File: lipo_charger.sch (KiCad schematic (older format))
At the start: 13 parts, among them P1 CONN_01X02, P2 CONN_01X02, Q1 BC557, Q2 BC547, U1 MCP73831

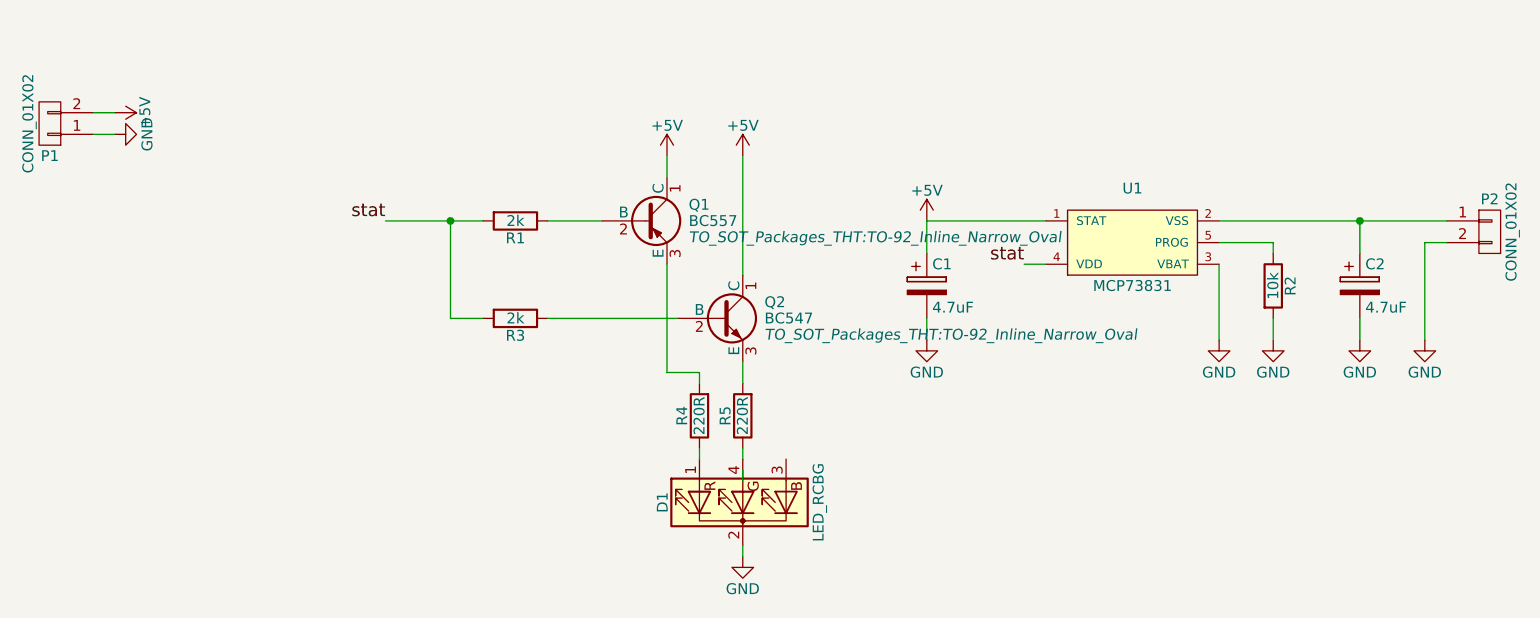
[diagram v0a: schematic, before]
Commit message: 3x lipo charger with tracks
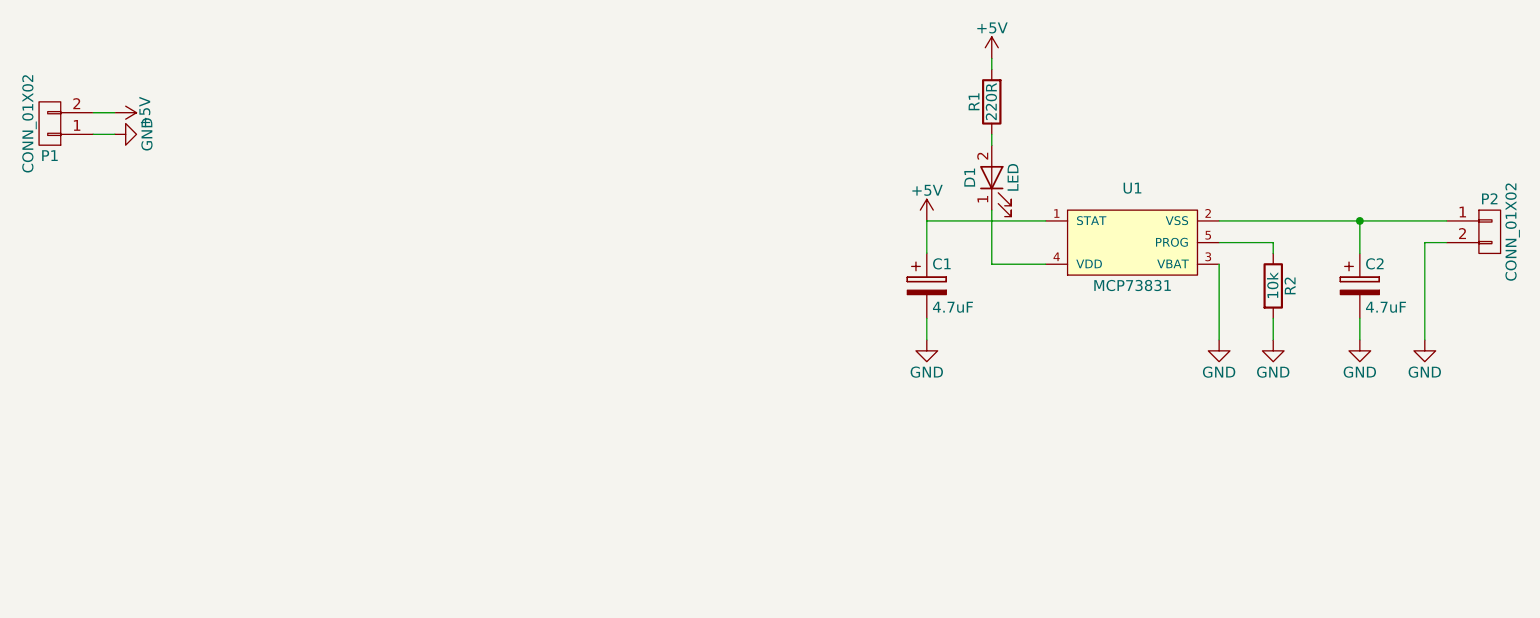
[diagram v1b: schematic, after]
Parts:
- removed D1: LED_RCBG, LEDs:LED_D5.0mm-4, symbol LED_RCBG
- removed Q1: BC557, TO_SOT_Packages_THT:TO-92_Inline_Narrow_Oval, symbol BC557
- removed Q2: BC547, TO_SOT_Packages_THT:TO-92_Inline_Narrow_Oval, symbol BC547
- removed R3: 2k, Resistors_ThroughHole:R_Axial_DIN0204_L3.6mm_D1.6mm_P5.08mm_Horizontal, symbol R
- removed R4, R5: 220R, Resistors_ThroughHole:R_Axial_DIN0204_L3.6mm_D1.6mm_P5.08mm_Horizontal, symbol R
- added D1: LED, LEDs:LED_D3.0mm, symbol LED
- P2: footprint borniers:bornier2_V -> Pin_Headers:Pin_Header_Straight_1x02_Pitch2.54mm
- R1: value 2k -> 220R
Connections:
- net labels removed: stat
- wire segments 30 -> 18
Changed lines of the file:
@@
 $EndDescr
-$Comp
-L LED_RCBG D1
-U 1 1 58917860
-P 4200 2600
-F 0 "D1" H 4200 2970 50  0000 C CNN
-F 1 "LED_RCBG" H 4200 2250 50  0000 C CNN
-F 2 "LEDs:LED_D5.0mm-4" H 4200 2550 50  0001 C CNN
-F 3 "" H 4200 2550 50  0000 C CNN
-	1    4200 2600
-	0    -1   -1   0
-$EndComp
-$Comp
-L R R1
-U 1 1 58917A5E
-P 3150 1300
-F 0 "R1" V 3230 1300 50  0000 C CNN
-F 1 "2k" V 3150 1300 50  0000 C CNN
-F 2 "Resistors_ThroughHole:R_Axial_DIN0204_L3.6mm_D1.6mm_P5.08mm_Horizontal" V 3080 1300 50  0001 C CNN
-F 3 "" H 3150 1300 50  0000 C CNN
-	1    3150 1300
-	0    1    1    0
-$EndComp
-$Comp
-L R R4
-U 1 1 58918266
-P 4000 2200
-F 0 "R4" V 4080 2200 50  0000 C CNN
-F 1 "220R" V 4000 2200 50  0000 C CNN
-F 2 "Resistors_ThroughHole:R_Axial_DIN0204_L3.6mm_D1.6mm_P5.08mm_Horizontal" V 3930 2200 50  0001 C CNN
-F 3 "" H 4000 2200 50  0000 C CNN
-	1    4000 2200
-	-1   0    0    1
-$EndComp
-$Comp
-L GND #PWR01
-U 1 1 5891833B
-P 4200 2850
-F 0 "#PWR01" H 4200 2600 50  0001 C CNN
-F 1 "GND" H 4200 2700 50  0000 C CNN
-F 2 "" H 4200 2850 50  0000 C CNN
-F 3 "" H 4200 2850 50  0000 C CNN
-	1    4200 2850
-	1    0    0    -1
-$EndComp
-Wire Wire Line
-	4200 2800 4200 2850
-Wire Wire Line
-	4200 2450 4200 2500
-Wire Wire Line
-	2550 1300 3000 1300
-Connection ~ 2850 1300
-Wire Wire Line
-	3300 1300 3550 1300
-$Comp
-L +5V #PWR02
-U 1 1 589185B2
-P 4200 1000
-F 0 "#PWR02" H 4200 850 50  0001 C CNN
-F 1 "+5V" H 4200 1140 50  0000 C CNN
-F 2 "" H 4200 1000 50  0000 C CNN
-F 3 "" H 4200 1000 50  0000 C CNN
-	1    4200 1000
-	1    0    0    -1
-$EndComp
-$Comp
-L +5V #PWR03
-U 1 1 589185DE
-P 3850 1000
-F 0 "#PWR03" H 3850 850 50  0001 C CNN
-F 1 "+5V" H 3850 1140 50  0000 C CNN
-F 2 "" H 3850 1000 50  0000 C CNN
-F 3 "" H 3850 1000 50  0000 C CNN
-	1    3850 1000
-	1    0    0    -1
-$EndComp
-Wire Wire Line
-	3850 1000 3850 1100
-Text Label 2550 1300 2    60   ~ 0
-stat
-$Comp
-L R R3
-U 1 1 58918F5F
-P 3150 1750
-F 0 "R3" V 3230 1750 50  0000 C CNN
-F 1 "2k" V 3150 1750 50  0000 C CNN
-F 2 "Resistors_ThroughHole:R_Axial_DIN0204_L3.6mm_D1.6mm_P5.08mm_Horizontal" V 3080 1750 50  0001 C CNN
-F 3 "" H 3150 1750 50  0000 C CNN
-	1    3150 1750
-	0    1    1    0
-$EndComp
-Wire Wire Line
-	3000 1750 2850 1750
-Wire Wire Line
-	3300 1750 3900 1750
-Wire Wire Line
-	3850 1500 3850 2000
-Wire Wire Line
-	3850 2000 4000 2000
-Wire Wire Line
-	4000 2000 4000 2050
-Wire Wire Line
-	4200 1950 4200 2050
-Wire Wire Line
-	4200 1000 4200 1550
-Wire Wire Line
-	2850 1750 2850 1300
 $Comp
 L MCP73831 U1
@@
 	1    0    0    1
 $EndComp
-Text Label 5500 1500 2    60   ~ 0
-stat
-Wire Wire Line
-	5600 1500 5500 1500
+Wire Wire Line
+	5350 1500 5600 1500
 $Comp
 L CP C1
@@
 	7050 1850 7050 1750
 $Comp
-L GND #PWR04
+L GND #PWR01
 U 1 1 589213B6
 P 6400 1850
-F 0 "#PWR04" H 6400 1600 50  0001 C CNN
+F 0 "#PWR01" H 6400 1600 50  0001 C CNN
 F 1 "GND" H 6400 1700 50  0000 C CNN
 F 2 "" H 6400 1850 50  0000 C CNN
@@
 $EndComp
 $Comp
-L GND #PWR05
+L GND #PWR02
 U 1 1 58921415
 P 6650 1850
-F 0 "#PWR05" H 6650 1600 50  0001 C CNN
+F 0 "#PWR02" H 6650 1600 50  0001 C CNN
 F 1 "GND" H 6650 1700 50  0000 C CNN
 F 2 "" H 6650 1850 50  0000 C CNN
@@
 $EndComp
 $Comp
-L GND #PWR06
+L GND #PWR03
 U 1 1 58921444
 P 7050 1850
-F 0 "#PWR06" H 7050 1600 50  0001 C CNN
+F 0 "#PWR03" H 7050 1600 50  0001 C CNN
 F 1 "GND" H 7050 1700 50  0000 C CNN
 F 2 "" H 7050 1850 50  0000 C CNN
@@
 F 0 "P2" H 7650 1500 50  0000 C CNN
 F 1 "CONN_01X02" V 7750 1350 50  0000 C CNN
-F 2 "borniers:bornier2_V" H 7650 1350 50  0001 C CNN
+F 2 "Pin_Headers:Pin_Header_Straight_1x02_Pitch2.54mm" H 7650 1350 50  0001 C CNN
 F 3 "" H 7650 1350 50  0000 C CNN
 	1    7650 1350
@@
 Connection ~ 7050 1300
 $Comp
-L GND #PWR07
+L GND #PWR04
 U 1 1 5892153A
 P 7350 1850
-F 0 "#PWR07" H 7350 1600 50  0001 C CNN
+F 0 "#PWR04" H 7350 1600 50  0001 C CNN
 F 1 "GND" H 7350 1700 50  0000 C CNN
 F 2 "" H 7350 1850 50  0000 C CNN
@@
 	5050 1300 5050 1450
 $Comp
-L GND #PWR08
+L GND #PWR05
 U 1 1 58921734
 P 5050 1850
-F 0 "#PWR08" H 5050 1600 50  0001 C CNN
+F 0 "#PWR05" H 5050 1600 50  0001 C CNN
 F 1 "GND" H 5050 1700 50  0000 C CNN
 F 2 "" H 5050 1850 50  0000 C CNN
@@
 $EndComp
 $Comp
-L GND #PWR09
+L GND #PWR06
 U 1 1 58921B30
 P 1300 900
-F 0 "#PWR09" H 1300 650 50  0001 C CNN
+F 0 "#PWR06" H 1300 650 50  0001 C CNN
 F 1 "GND" H 1300 750 50  0000 C CNN
 F 2 "" H 1300 900 50  0000 C CNN
@@
 	1200 800  1300 800
 $Comp
-L +5V #PWR010
+L +5V #PWR07
 U 1 1 58921C6A
 P 1300 800
-F 0 "#PWR010" H 1300 650 50  0001 C CNN
+F 0 "#PWR07" H 1300 650 50  0001 C CNN
 F 1 "+5V" H 1300 940 50  0000 C CNN
 F 2 "" H 1300 800 50  0000 C CNN
@@
 $EndComp
 $Comp
-L +5V #PWR011
+L +5V #PWR08
 U 1 1 58921CFE
 P 5050 1300
-F 0 "#PWR011" H 5050 1150 50  0001 C CNN
+F 0 "#PWR08" H 5050 1150 50  0001 C CNN
 F 1 "+5V" H 5050 1440 50  0000 C CNN
 F 2 "" H 5050 1300 50  0000 C CNN
@@
 $EndComp
 $Comp
-L BC547 Q2
-U 1 1 5892297D
-P 4100 1750
-F 0 "Q2" H 4300 1825 50  0000 L CNN
-F 1 "BC547" H 4300 1750 50  0000 L CNN
-F 2 "TO_SOT_Packages_THT:TO-92_Inline_Narrow_Oval" H 4300 1675 50  0000 L CIN
-F 3 "" H 4100 1750 50  0000 L CNN
-	1    4100 1750
-	1    0    0    -1
-$EndComp
-$Comp
-L BC557 Q1
-U 1 1 58922A4A
-P 3750 1300
-F 0 "Q1" H 3950 1375 50  0000 L CNN
-F 1 "BC557" H 3950 1300 50  0000 L CNN
-F 2 "TO_SOT_Packages_THT:TO-92_Inline_Narrow_Oval" H 3950 1225 50  0000 L CIN
-F 3 "" H 3750 1300 50  0000 L CNN
-	1    3750 1300
-	1    0    0    -1
-$EndComp
-$Comp
-L R R5
-U 1 1 58922F1E
-P 4200 2200
-F 0 "R5" V 4280 2200 50  0000 C CNN
-F 1 "220R" V 4200 2200 50  0000 C CNN
-F 2 "Resistors_ThroughHole:R_Axial_DIN0204_L3.6mm_D1.6mm_P5.08mm_Horizontal" V 4130 2200 50  0001 C CNN
-F 3 "" H 4200 2200 50  0000 C CNN
-	1    4200 2200
+L LED D1
+U 1 1 589419EB
+P 5350 1100
+F 0 "D1" H 5350 1200 50  0000 C CNN
+F 1 "LED" H 5350 1000 50  0000 C CNN
+F 2 "LEDs:LED_D3.0mm" H 5350 1100 50  0001 C CNN
+F 3 "" H 5350 1100 50  0000 C CNN
+	1    5350 1100
+	0    -1   -1   0
+$EndComp
+$Comp
+L R R1
+U 1 1 58941BC2
+P 5350 750
+F 0 "R1" V 5430 750 50  0000 C CNN
+F 1 "220R" V 5350 750 50  0000 C CNN
+F 2 "Resistors_ThroughHole:R_Axial_DIN0204_L3.6mm_D1.6mm_P5.08mm_Horizontal" V 5280 750 50  0001 C CNN
+F 3 "" H 5350 750 50  0000 C CNN
+	1    5350 750
 	-1   0    0    1
 $EndComp
 Wire Wire Line
-	4000 2350 4000 2400
-Wire Wire Line
-	4200 2350 4200 2400
+	5350 1500 5350 1250
+Wire Wire Line
+	5350 950  5350 900
+Wire Wire Line
+	5350 600  5350 550
+$Comp
+L +5V #PWR09
+U 1 1 58941E86
+P 5350 550
+F 0 "#PWR09" H 5350 400 50  0001 C CNN
+F 1 "+5V" H 5350 690 50  0000 C CNN
+F 2 "" H 5350 550 50  0000 C CNN
+F 3 "" H 5350 550 50  0000 C CNN
+	1    5350 550
+	1    0    0    -1
+$EndComp
 $EndSCHEMATC
